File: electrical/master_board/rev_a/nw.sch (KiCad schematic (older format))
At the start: 21 parts, among them CN106 BRIDGE_NW_OUTER;M1x2+M2x5, CN70 HCSR04H;F1X4, Q4 2N7000;SOT23, Q5 2N7000;SOT23, Q6 2N7000;SOT23

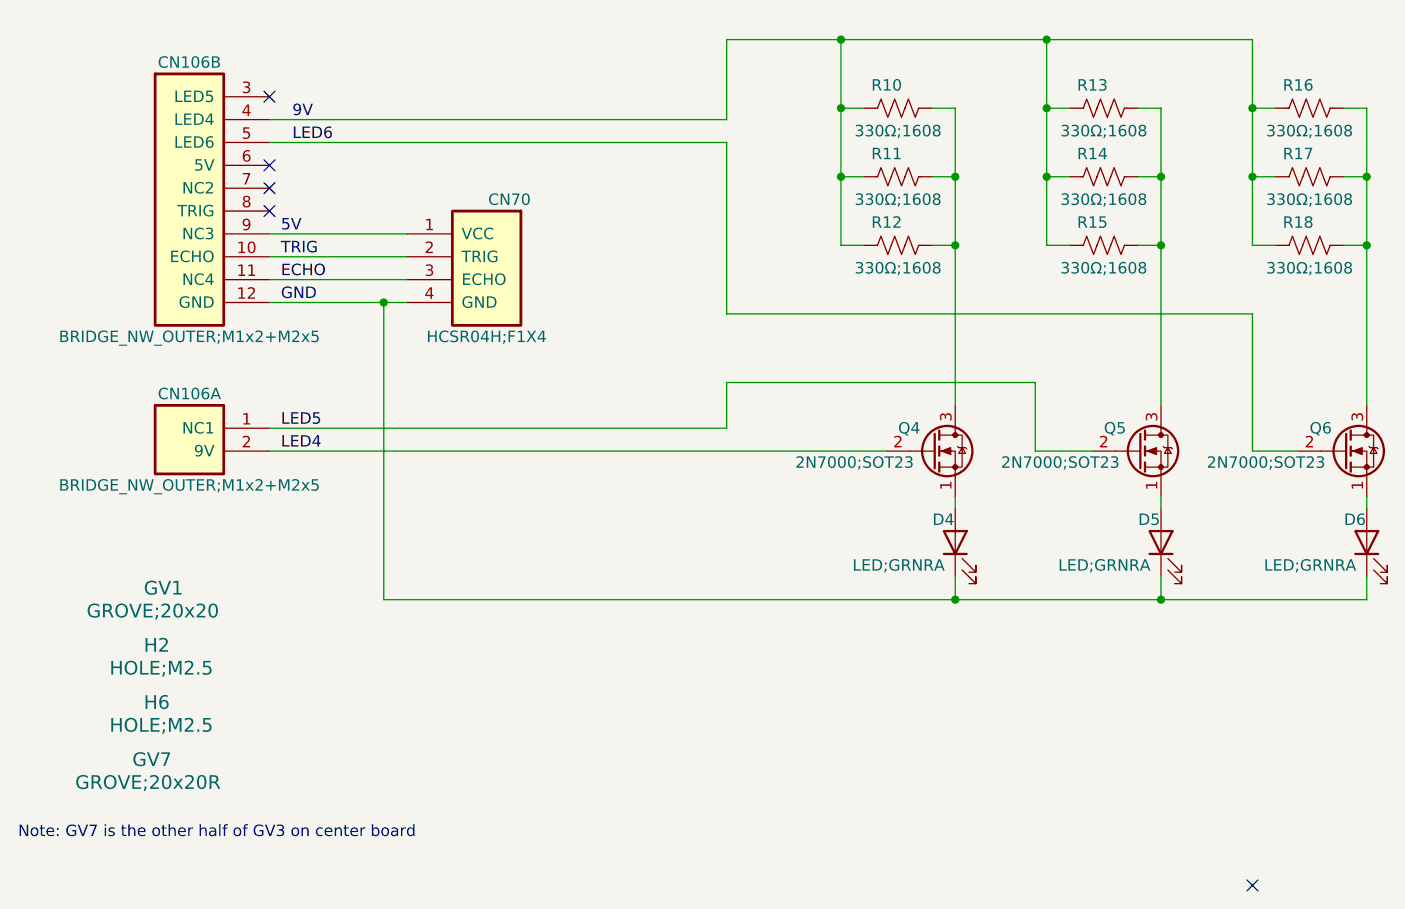
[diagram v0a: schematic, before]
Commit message: Redid the pins on the NW PCB.
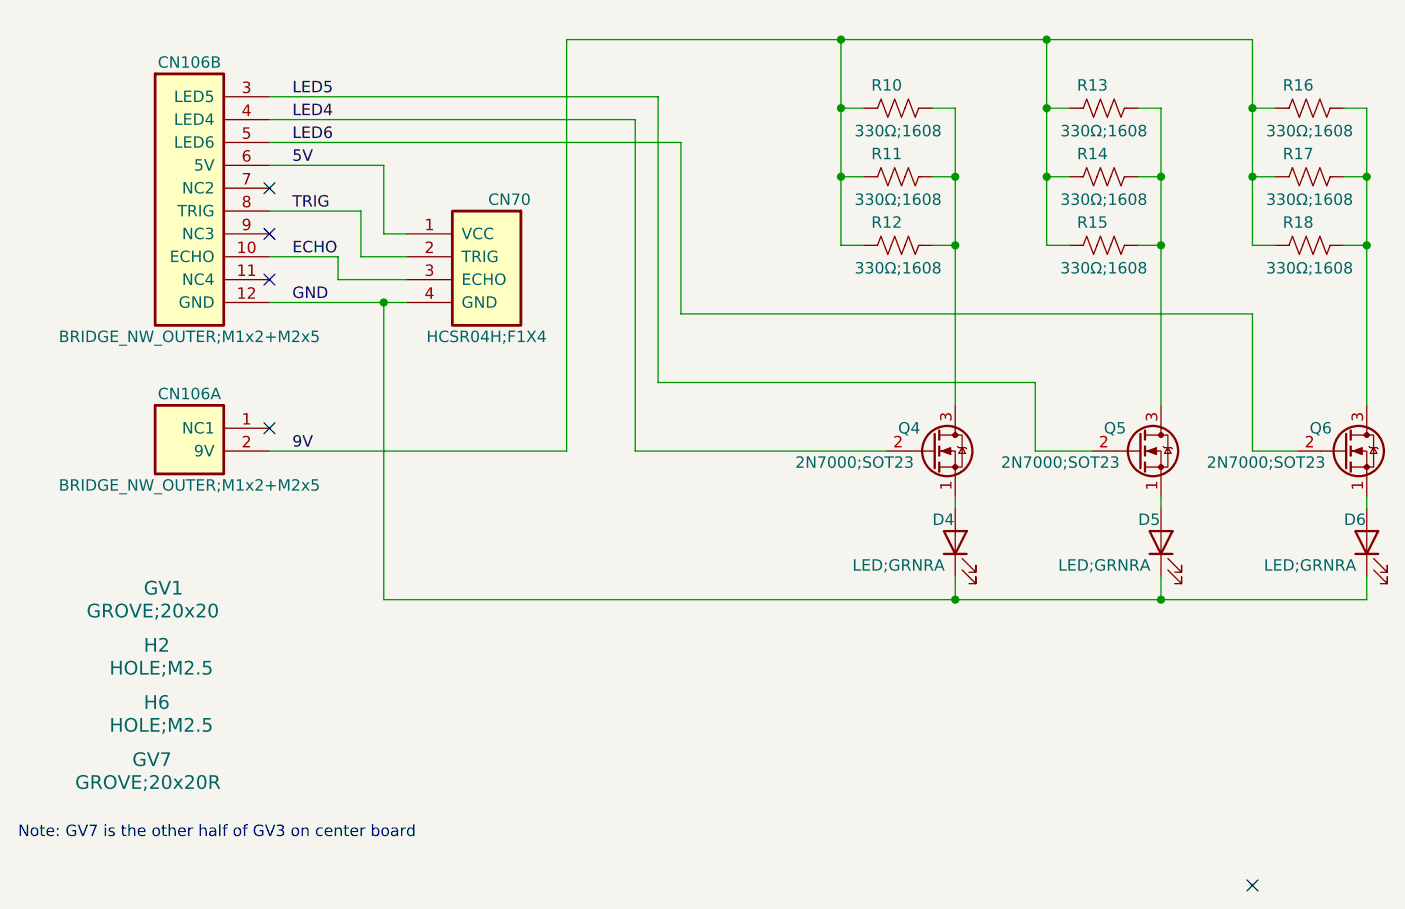
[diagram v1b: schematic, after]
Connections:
- net 5V: now also CN106.6 (5V); no longer CN106.9 (NC3)
- net 9V: now also CN106.2 (9V); no longer CN106.4 (LED4)
- net ECHO: now also CN106.10 (ECHO); no longer CN106.11 (NC4)
- net LED4: now also CN106.4 (LED4); no longer CN106.2 (9V)
- net LED5: now also CN106.3 (LED5); no longer CN106.1 (NC1)
- net TRIG: now also CN106.8 (TRIG); no longer CN106.10 (ECHO)
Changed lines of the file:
@@
 	1    0    0    -1
 $EndComp
-Text Label 2050 3750 0    50   ~ 0
+Text Label 2100 3750 0    50   ~ 0
 GND
 $Comp
@@
 Connection ~ 5900 5050
 Wire Wire Line
-	4000 3800 6300 3800
-Wire Wire Line
 	6300 3800 6300 4400
 Wire Wire Line
@@
 	2500 5050 5000 5050
 Connection ~ 5000 5050
-Text Label 2050 4300 0    50   ~ 0
+Text Label 2100 2850 0    50   ~ 0
 LED5
 Wire Wire Line
 	5350 4100 5350 4400
-Wire Wire Line
-	4000 4100 5350 4100
-Text Label 2050 4400 0    50   ~ 0
+Text Label 2100 2950 0    50   ~ 0
 LED4
 Text Label 2100 3050 0    50   ~ 0
 LED6
-Text Label 2050 3550 0    50   ~ 0
+Text Label 2100 3350 0    50   ~ 0
 TRIG
-Text Label 2050 3450 0    50   ~ 0
+Text Label 2100 3150 0    50   ~ 0
 5V
-Text Label 2050 3650 0    50   ~ 0
+Text Label 2100 3550 0    50   ~ 0
 ECHO
 NoConn ~ 6300 6300
-Wire Wire Line
-	2000 3750 2500 3750
 Wire Wire Line
 	2500 3750 2500 5050
@@
 $EndComp
 Wire Wire Line
-	2000 3450 2600 3450
-Wire Wire Line
-	2000 3550 2600 3550
-Wire Wire Line
-	2000 3650 2600 3650
-Wire Wire Line
 	2600 3750 2500 3750
+Connection ~ 4500 2600
+Text Label 2100 4400 0    50   ~ 0
+9V
+Wire Wire Line
+	2000 4400 3300 4400
+Wire Wire Line
+	3300 4400 3300 2600
+Wire Wire Line
+	3300 2600 4500 2600
+Wire Wire Line
+	2000 3750 2500 3750
 Connection ~ 2500 3750
 Wire Wire Line
-	2000 4400 4700 4400
-Wire Wire Line
-	2000 4300 4000 4300
-Wire Wire Line
-	4000 4300 4000 4100
-Wire Wire Line
-	2000 2950 4000 2950
-Wire Wire Line
-	4000 2950 4000 2600
-Wire Wire Line
-	4000 2600 4500 2600
-Connection ~ 4500 2600
-Text Label 2100 2950 0    50   ~ 0
-9V
-NoConn ~ 2000 3150
+	2000 3550 2300 3550
+Wire Wire Line
+	2300 3550 2300 3650
+Wire Wire Line
+	2300 3650 2600 3650
+Wire Wire Line
+	2000 3350 2400 3350
+Wire Wire Line
+	2400 3350 2400 3550
+Wire Wire Line
+	2400 3550 2600 3550
+Wire Wire Line
+	2600 3450 2500 3450
+Wire Wire Line
+	2500 3450 2500 3150
+Wire Wire Line
+	2500 3150 2000 3150
+Wire Wire Line
+	2000 2950 3600 2950
+Wire Wire Line
+	3600 2950 3600 4400
+Wire Wire Line
+	3600 4400 4700 4400
+Wire Wire Line
+	2000 2850 3700 2850
+Wire Wire Line
+	3700 2850 3700 4100
+Wire Wire Line
+	3700 4100 5350 4100
+Wire Wire Line
+	2000 3050 3800 3050
+Wire Wire Line
+	3800 3050 3800 3800
+Wire Wire Line
+	3800 3800 6300 3800
 NoConn ~ 2000 3250
-NoConn ~ 2000 3350
-NoConn ~ 2000 2850
-Wire Wire Line
-	2000 3050 4000 3050
-Wire Wire Line
-	4000 3050 4000 3800
+NoConn ~ 2000 3450
+NoConn ~ 2000 3650
+NoConn ~ 2000 4300
 $EndSCHEMATC

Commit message: Linked the NE/NW/SE/SW sheets to master_board.
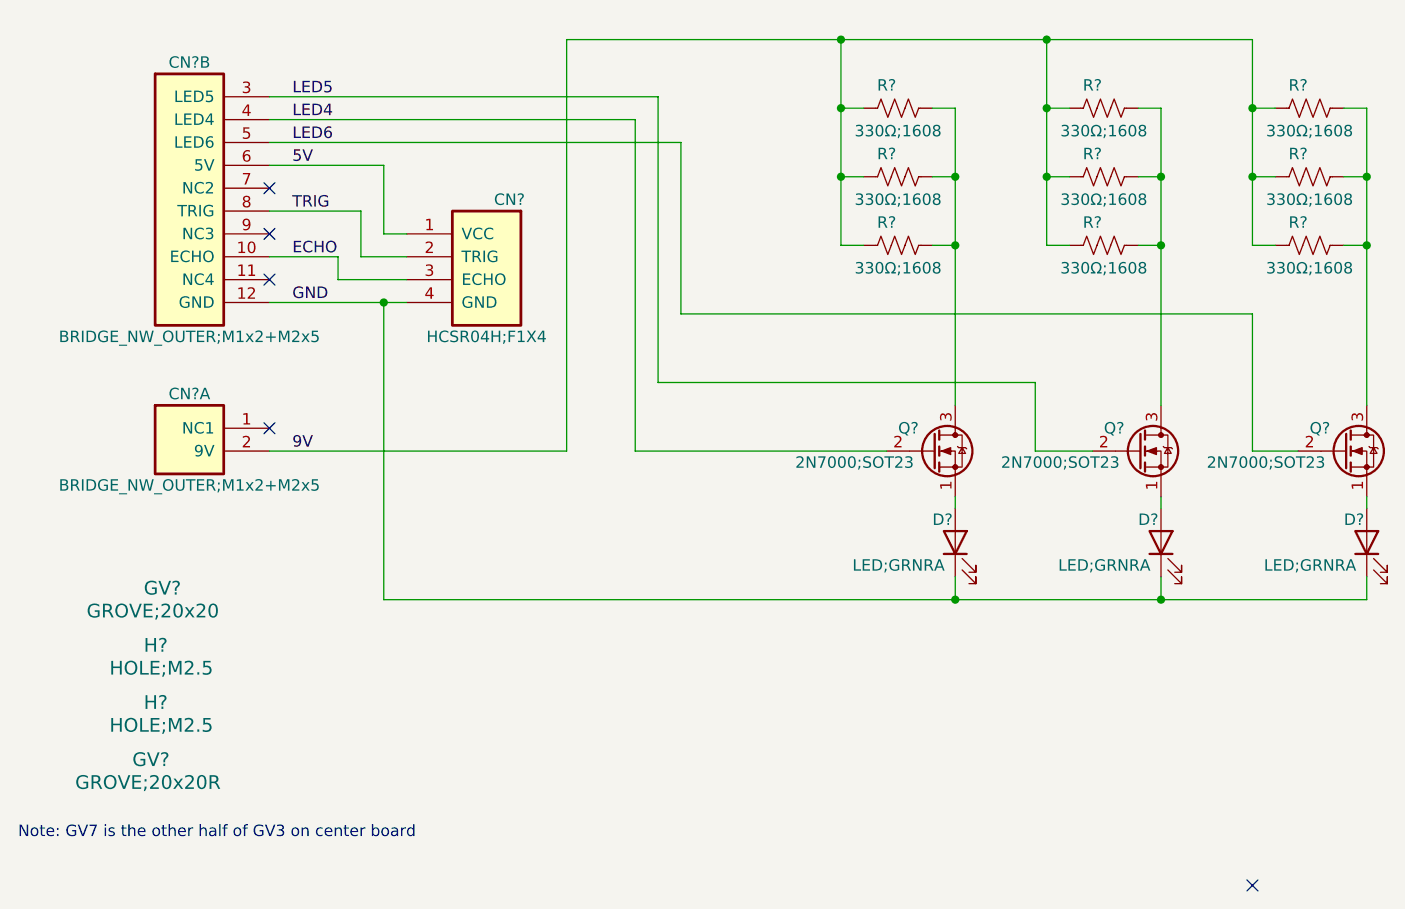
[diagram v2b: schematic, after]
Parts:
- renumbered CN70 to CN?, CN106 to CN?, D4 to D?, D5 to D?, D6 to D?, GV1 to GV?, GV7 to GV?, H6 to H?, H2 to H?, Q4 to Q?, Q5 to Q?, Q6 to Q?, R12 to R?, R11 to R?, R10 to R?, R15 to R?, R14 to R?, R13 to R?, R18 to R?, R17 to R?, R16 to R?
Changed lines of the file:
@@
 $Descr A 11000 8500
 encoding utf-8
-Sheet 1 1
+Sheet 12 12
 Title "HR2 NE PCB"
 Date "2020-06-13"
@@
 $EndDescr
 $Comp
-L HR2:HOLE;M2.5 H6
+L HR2:HOLE;M2.5 H?
 U 1 1 5F2F7B9C
 P 1500 5550
-F 0 "H6" H 1450 5600 60  0000 L CNN
+F 0 "H?" H 1450 5600 60  0000 L CNN
 F 1 "HOLE;M2.5" H 1300 5500 60  0000 L CNN
 F 2 "MountingHole:MountingHole_2.7mm_M2.5" H 1700 5600 60  0001 L CNN
@@
 $EndComp
 $Comp
-L HR2:HOLE;M2.5 H2
+L HR2:HOLE;M2.5 H?
 U 1 1 5F2F8125
 P 1500 5300
-F 0 "H2" H 1450 5350 60  0000 L CNN
+F 0 "H?" H 1450 5350 60  0000 L CNN
 F 1 "HOLE;M2.5" H 1300 5250 60  0000 L CNN
 F 2 "MountingHole:MountingHole_2.7mm_M2.5" H 1700 5350 60  0001 L CNN
@@
 $EndComp
 $Comp
-L HR2:GROVE;20x20 GV1
+L HR2:GROVE;20x20 GV?
 U 1 1 5F2F999C
 P 1500 5050
-F 0 "GV1" H 1450 5100 60  0000 L CNN
+F 0 "GV?" H 1450 5100 60  0000 L CNN
 F 1 "GROVE;20x20" H 1200 5000 60  0000 L CNN
 F 2 "HR2:GROVE20x20" H 1700 5100 60  0001 L CNN
@@
 $EndComp
 $Comp
-L HR2:GROVE;20x20R GV7
+L HR2:GROVE;20x20R GV?
 U 1 1 5F303BB1
 P 1500 5800
-F 0 "GV7" H 1400 5850 60  0000 L CNN
+F 0 "GV?" H 1400 5850 60  0000 L CNN
 F 1 "GROVE;20x20R" H 1150 5750 60  0000 L CNN
 F 2 "HR2:GROVE20x20R" H 1700 5850 60  0001 L CNN
@@
 Note: GV7 is the other half of GV3 on center board
 $Comp
-L Device:LED D4
+L Device:LED D?
 U 1 1 5F30BC5B
 P 5000 4800
-F 0 "D4" V 5100 4900 50  0000 R CNN
+F 0 "D?" V 5100 4900 50  0000 R CNN
 F 1 "LED;GRNRA" V 4900 5250 50  0000 R CNN
 F 2 "HR2:LED_GRNRA" H 5000 4800 50  0001 C CNN
@@
 $EndComp
 $Comp
-L Device:LED D5
+L Device:LED D?
 U 1 1 5F30DD43
 P 5900 4800
-F 0 "D5" V 6000 4900 50  0000 R CNN
+F 0 "D?" V 6000 4900 50  0000 R CNN
 F 1 "LED;GRNRA" V 5800 5250 50  0000 R CNN
 F 2 "HR2:LED_GRNRA" H 5900 4800 50  0001 C CNN
@@
 $EndComp
 $Comp
-L Device:LED D6
+L Device:LED D?
 U 1 1 5F30E439
 P 6800 4800
-F 0 "D6" V 6900 4900 50  0000 R CNN
+F 0 "D?" V 6900 4900 50  0000 R CNN
 F 1 "LED;GRNRA" V 6700 5250 50  0000 R CNN
 F 2 "HR2:LED_GRNRA" H 6800 4800 50  0001 C CNN
@@
 $EndComp
 $Comp
-L HR2:BRIDGE_NW_OUTER;M1x2+M2x5 CN106
+L HR2:BRIDGE_NW_OUTER;M1x2+M2x5 CN?
 U 1 1 5F3877C6
 P 1300 4300
-F 0 "CN106" H 1650 4450 50  0000 C CNN
+F 0 "CN?" H 1650 4450 50  0000 C CNN
 F 1 "BRIDGE_NW_OUTER;M1x2+M2x5" H 1650 4050 50  0000 C CNN
 F 2 "HR2:BRIDGE_NW_OUTER_M1x2+M2x5" H 1500 4350 60  0001 L CNN
@@
 $EndComp
 $Comp
-L HR2:BRIDGE_NW_OUTER;M1x2+M2x5 CN106
+L HR2:BRIDGE_NW_OUTER;M1x2+M2x5 CN?
 U 2 1 5F389BE1
 P 1300 2850
-F 0 "CN106" H 1650 3000 50  0000 C CNN
+F 0 "CN?" H 1650 3000 50  0000 C CNN
 F 1 "BRIDGE_NW_OUTER;M1x2+M2x5" H 1650 1800 50  0000 C CNN
 F 2 "HR2:BRIDGE_NW_OUTER_M1x2+M2x5" H 1500 2900 60  0001 L CNN
@@
 GND
 $Comp
-L Transistor_FET:2N7000 Q4
+L Transistor_FET:2N7000 Q?
 U 1 1 5F433B12
 P 4900 4400
-F 0 "Q4" H 4750 4500 50  0000 L CNN
+F 0 "Q?" H 4750 4500 50  0000 L CNN
 F 1 "2N7000;SOT23" H 4300 4350 50  0000 L CNN
 F 2 "Package_TO_SOT_SMD:SOT-23" H 5100 4325 50  0001 L CIN
@@
 $EndComp
 $Comp
-L Device:R_US R12
+L Device:R_US R?
 U 1 1 5F434F01
 P 4750 3500
-F 0 "R12" V 4650 3450 50  0000 C CNN
+F 0 "R?" V 4650 3450 50  0000 C CNN
 F 1 "330Ω;1608" V 4850 3500 50  0000 C CNN
 F 2 "Resistor_SMD:R_0603_1608Metric" V 4790 3490 50  0001 C CNN
@@
 $EndComp
 $Comp
-L Device:R_US R11
+L Device:R_US R?
 U 1 1 5F437EB2
 P 4750 3200
-F 0 "R11" V 4650 3150 50  0000 C CNN
+F 0 "R?" V 4650 3150 50  0000 C CNN
 F 1 "330Ω;1608" V 4850 3200 50  0000 C CNN
 F 2 "Resistor_SMD:R_0603_1608Metric" V 4790 3190 50  0001 C CNN
@@
 $EndComp
 $Comp
-L Device:R_US R10
+L Device:R_US R?
 U 1 1 5F43808D
 P 4750 2900
-F 0 "R10" V 4650 2850 50  0000 C CNN
+F 0 "R?" V 4650 2850 50  0000 C CNN
 F 1 "330Ω;1608" V 4850 2900 50  0000 C CNN
 F 2 "Resistor_SMD:R_0603_1608Metric" V 4790 2890 50  0001 C CNN
@@
 Connection ~ 4500 2900
 $Comp
-L Transistor_FET:2N7000 Q5
+L Transistor_FET:2N7000 Q?
 U 1 1 5F43B291
 P 5800 4400
-F 0 "Q5" H 5650 4500 50  0000 L CNN
+F 0 "Q?" H 5650 4500 50  0000 L CNN
 F 1 "2N7000;SOT23" H 5200 4350 50  0000 L CNN
 F 2 "Package_TO_SOT_SMD:SOT-23" H 6000 4325 50  0001 L CIN
@@
 $EndComp
 $Comp
-L Device:R_US R15
+L Device:R_US R?
 U 1 1 5F43B29B
 P 5650 3500
-F 0 "R15" V 5550 3450 50  0000 C CNN
+F 0 "R?" V 5550 3450 50  0000 C CNN
 F 1 "330Ω;1608" V 5750 3500 50  0000 C CNN
 F 2 "Resistor_SMD:R_0603_1608Metric" V 5690 3490 50  0001 C CNN
@@
 $EndComp
 $Comp
-L Device:R_US R14
+L Device:R_US R?
 U 1 1 5F43B2A5
 P 5650 3200
-F 0 "R14" V 5550 3150 50  0000 C CNN
+F 0 "R?" V 5550 3150 50  0000 C CNN
 F 1 "330Ω;1608" V 5750 3200 50  0000 C CNN
 F 2 "Resistor_SMD:R_0603_1608Metric" V 5690 3190 50  0001 C CNN
@@
 $EndComp
 $Comp
-L Device:R_US R13
+L Device:R_US R?
 U 1 1 5F43B2AF
 P 5650 2900
-F 0 "R13" V 5550 2850 50  0000 C CNN
+F 0 "R?" V 5550 2850 50  0000 C CNN
 F 1 "330Ω;1608" V 5750 2900 50  0000 C CNN
 F 2 "Resistor_SMD:R_0603_1608Metric" V 5690 2890 50  0001 C CNN
@@
 Connection ~ 5400 2900
 $Comp
-L Transistor_FET:2N7000 Q6
+L Transistor_FET:2N7000 Q?
 U 1 1 5F4407CF
 P 6700 4400
-F 0 "Q6" H 6550 4500 50  0000 L CNN
+F 0 "Q?" H 6550 4500 50  0000 L CNN
 F 1 "2N7000;SOT23" H 6100 4350 50  0000 L CNN
 F 2 "Package_TO_SOT_SMD:SOT-23" H 6900 4325 50  0001 L CIN
@@
 $EndComp
 $Comp
-L Device:R_US R18
+L Device:R_US R?
 U 1 1 5F4407D9
 P 6550 3500
-F 0 "R18" V 6450 3450 50  0000 C CNN
+F 0 "R?" V 6450 3450 50  0000 C CNN
 F 1 "330Ω;1608" V 6650 3500 50  0000 C CNN
 F 2 "Resistor_SMD:R_0603_1608Metric" V 6590 3490 50  0001 C CNN
@@
 $EndComp
 $Comp
-L Device:R_US R17
+L Device:R_US R?
 U 1 1 5F4407E3
 P 6550 3200
-F 0 "R17" V 6450 3150 50  0000 C CNN
+F 0 "R?" V 6450 3150 50  0000 C CNN
 F 1 "330Ω;1608" V 6650 3200 50  0000 C CNN
 F 2 "Resistor_SMD:R_0603_1608Metric" V 6590 3190 50  0001 C CNN
@@
 $EndComp
 $Comp
-L Device:R_US R16
+L Device:R_US R?
 U 1 1 5F4407ED
 P 6550 2900
-F 0 "R16" V 6450 2850 50  0000 C CNN
+F 0 "R?" V 6450 2850 50  0000 C CNN
 F 1 "330Ω;1608" V 6650 2900 50  0000 C CNN
 F 2 "Resistor_SMD:R_0603_1608Metric" V 6590 2890 50  0001 C CNN
@@
 	2500 3750 2500 5050
 $Comp
-L HR2:HCSR04H;F1X4 CN70
+L HR2:HCSR04H;F1X4 CN?
 U 1 1 5F0B8A7B
 P 3300 3450
-F 0 "CN70" H 3550 3600 50  0000 C CNN
+F 0 "CN?" H 3550 3600 50  0000 C CNN
 F 1 "HCSR04H;F1X4" H 3650 3000 50  0000 C CNN
 F 2 "HR2:HCSR04_F1x4H" H 3500 3500 60  0001 L CNN
